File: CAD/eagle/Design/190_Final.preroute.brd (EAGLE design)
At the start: 160 x 100 mm, 29 parts, among them U1_0_BRAIN ADAFRUIT-PRO-TRINKET-5V-BOB, U1_6_CASTER CASTERADAFRUIT-3/4IN, U1_7_CASTER_2 CASTERADAFRUIT-3/4IN

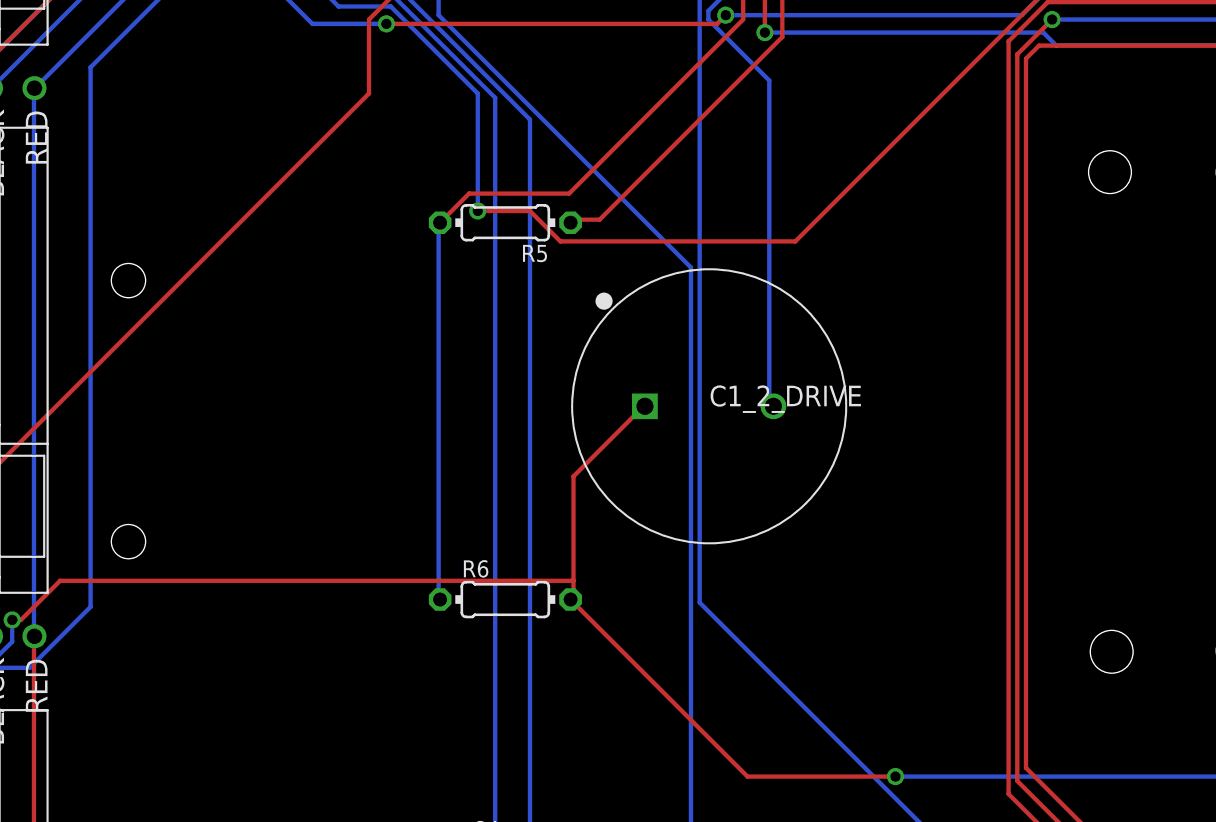
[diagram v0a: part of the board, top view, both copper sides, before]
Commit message: Added state machine to robot
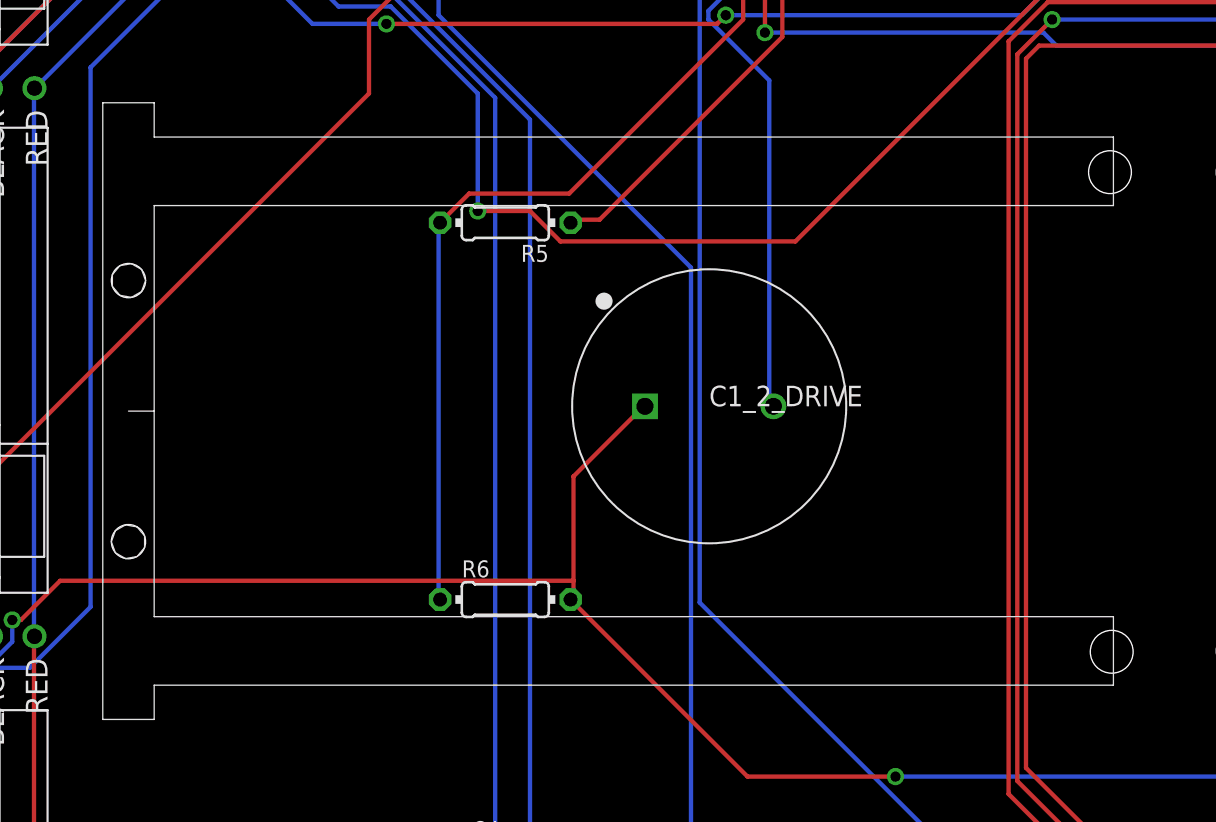
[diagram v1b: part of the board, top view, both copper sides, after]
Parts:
- added U$4: (no value), 3DPrintedParts:IRSTAND
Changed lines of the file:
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@@
 <?xml version="1.0" encoding="utf-8"?>
 <!DOCTYPE eagle SYSTEM "eagle.dtd">
-<eagle version="7.2.0">
+<eagle version="7.5.0">
 <drawing>
 <settings>
@@
 <setting verticaltext="up"/>
 </settings>
-<grid distance="1" unitdist="mm" unit="mm" style="lines" multiple="1" display="no" altdistance="0.1" altunitdist="mm" altunit="mm"/>
+<grid distance="0.5" unitdist="mm" unit="mm" style="lines" multiple="1" display="no" altdistance="0.1" altunitdist="mm" altunit="mm"/>
 <layers>
 <layer number="1" name="Top" color="4" fill="1" visible="yes" active="yes"/>
@@
 <wire x1="80" y1="-50" x2="-80" y2="-50" width="0.254" layer="20"/>
 <wire x1="80" y1="50" x2="80" y2="-50" width="0.254" layer="20"/>
+<dimension x1="-1.5" y1="-14.5" x2="-1.5" y2="13.5" x3="-1.5" y3="-0.5" textsize="1.778" layer="20"/>
+<dimension x1="-1.5" y1="0" x2="-59" y2="0" x3="-30.25" y3="0" textsize="1.778" layer="20" dtype="horizontal"/>
+<dimension x1="-59" y1="0" x2="-59" y2="-8" x3="-59" y3="-4" textsize="1.778" layer="20"/>
+<dimension x1="-59" y1="0" x2="-59" y2="8" x3="-59" y3="4" textsize="1.778" layer="20" dtype="vertical"/>
 </plain>
 <attributes>
@@
 <element name="R5" library="resistor" package="0204/7" value="" x="-37" y="11" rot="R180"/>
 <element name="R6" library="resistor" package="0204/7" value="" x="-37" y="-11"/>
+<element name="U$4" library="3DPrintedParts" package="IRSTAND" value="" x="-59" y="0"/>
 </elements>
 <signals>
